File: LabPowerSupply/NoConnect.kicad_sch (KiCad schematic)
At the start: 2 parts

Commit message: another commit
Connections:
- net GND1: now reaches Inverter1.11
- net GND1: now also Inverter1.13, Inverter1.3, Inverter1.5, Inverter1.9
- net GND2: now reaches Inverter2.9
- net GND2: now also Inverter2.11, Inverter2.13
- no-connect marks 16 -> 8
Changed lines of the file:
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@@
     (rev "1")
     (company "George Mason University")
-    (comment 4 "This sheet is for the invertes not used in the circuit.")
+    (comment 4 "This sheet is for the inverters not used in the circuit.")
+  )
+  (junction (at 102.87 78.74) (diameter 0) (color 0 0 0 0)
+  )
+  (junction (at 140.97 78.74) (diameter 0) (color 0 0 0 0)
+  )
+  (junction (at 102.87 120.65) (diameter 0) (color 0 0 0 0)
+  )
+  (junction (at 102.87 92.71) (diameter 0) (color 0 0 0 0)
+  )
+  (junction (at 102.87 106.68) (diameter 0) (color 0 0 0 0)
+  )
+  (junction (at 140.97 92.71) (diameter 0) (color 0 0 0 0)
   )
   (no_connect (at 118.11 78.74))
-  (no_connect (at 102.87 78.74))
-  (no_connect (at 102.87 64.77))
   (no_connect (at 118.11 64.77))
   (no_connect (at 156.21 64.77))
-  (no_connect (at 140.97 64.77))
-  (no_connect (at 140.97 78.74))
   (no_connect (at 156.21 78.74))
   (no_connect (at 156.21 92.71))
-  (no_connect (at 140.97 92.71))
-  (no_connect (at 102.87 120.65))
   (no_connect (at 118.11 120.65))
   (no_connect (at 118.11 106.68))
-  (no_connect (at 102.87 106.68))
-  (no_connect (at 102.87 92.71))
   (no_connect (at 118.11 92.71))
+  (wire (pts (xy 140.97 78.74) (xy 140.97 92.71))
+    (stroke (width 0) (type default) (color 0 0 0 0))
+  )
+  (wire (pts (xy 102.87 120.65) (xy 100.33 120.65))
+    (stroke (width 0) (type default) (color 0 0 0 0))
+  )
+  (wire (pts (xy 102.87 64.77) (xy 102.87 78.74))
+    (stroke (width 0) (type default) (color 0 0 0 0))
+  )
+  (wire (pts (xy 140.97 64.77) (xy 140.97 78.74))
+    (stroke (width 0) (type default) (color 0 0 0 0))
+  )
+  (wire (pts (xy 102.87 78.74) (xy 102.87 92.71))
+    (stroke (width 0) (type default) (color 0 0 0 0))
+  )
+  (wire (pts (xy 102.87 106.68) (xy 102.87 120.65))
+    (stroke (width 0) (type default) (color 0 0 0 0))
+  )
+  (wire (pts (xy 102.87 92.71) (xy 102.87 106.68))
+    (stroke (width 0) (type default) (color 0 0 0 0))
+  )
+  (wire (pts (xy 140.97 92.71) (xy 138.43 92.71))
+    (stroke (width 0) (type default) (color 0 0 0 0))
+  )
+  (hierarchical_label "GND2" (shape input) (at 138.43 92.71 180)
+    (effects (font (size 1.27 1.27)) (justify right))
+  )
+  (hierarchical_label "GND1" (shape input) (at 100.33 120.65 180)
+    (effects (font (size 1.27 1.27)) (justify right))
+  )
   (symbol (lib_id "74xx:74AHC04") (at 110.49 106.68 0) (unit 5)
     (in_bom yes) (on_board yes) (fields_autoplaced)

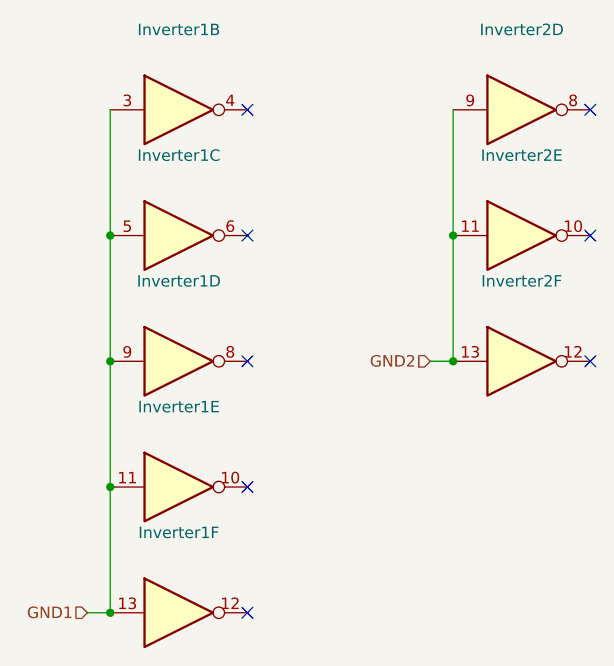
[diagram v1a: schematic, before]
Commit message: Made oscillator caps smd
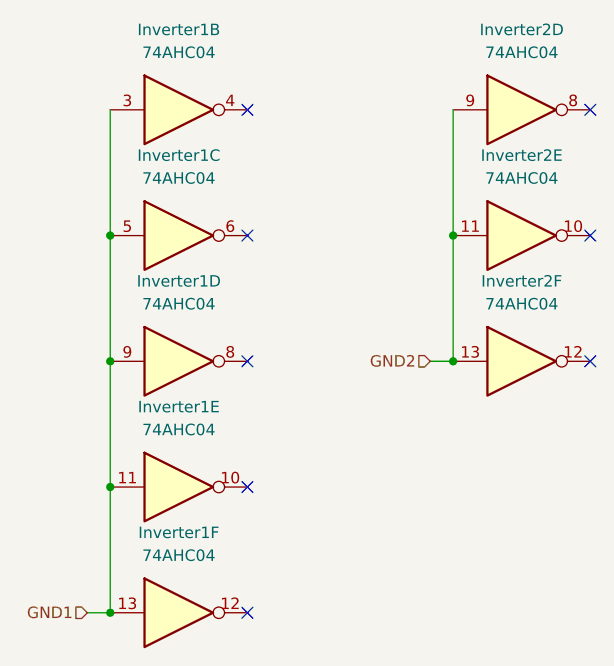
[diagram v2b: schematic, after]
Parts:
- Inverter1, Inverter2: value (none) -> 74AHC04; footprint (none) -> Package_DIP:DIP-14_W7.62mm
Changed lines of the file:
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@@
     (in_bom yes) (on_board yes) (fields_autoplaced)
     (property "Reference" "Inverter1" (id 0) (at 110.49 97.79 0))
-    (property "Value" "" (id 1) (at 110.49 100.33 0))
-    (property "Footprint" "" (id 2) (at 110.49 106.68 0)
+    (property "Value" "74AHC04" (id 1) (at 110.49 100.33 0))
+    (property "Footprint" "Package_DIP:DIP-14_W7.62mm" (id 2) (at 110.49 106.68 0)
       (effects (font (size 1.27 1.27)) hide)
     )
@@
     (in_bom yes) (on_board yes) (fields_autoplaced)
     (property "Reference" "Inverter1" (id 0) (at 110.49 111.76 0))
-    (property "Value" "" (id 1) (at 110.49 114.3 0))
-    (property "Footprint" "" (id 2) (at 110.49 120.65 0)
+    (property "Value" "74AHC04" (id 1) (at 110.49 114.3 0))
+    (property "Footprint" "Package_DIP:DIP-14_W7.62mm" (id 2) (at 110.49 120.65 0)
       (effects (font (size 1.27 1.27)) hide)
     )
@@
     (in_bom yes) (on_board yes) (fields_autoplaced)
     (property "Reference" "Inverter1" (id 0) (at 110.49 69.85 0))
-    (property "Value" "" (id 1) (at 110.49 72.39 0))
-    (property "Footprint" "" (id 2) (at 110.49 78.74 0)
+    (property "Value" "74AHC04" (id 1) (at 110.49 72.39 0))
+    (property "Footprint" "Package_DIP:DIP-14_W7.62mm" (id 2) (at 110.49 78.74 0)
       (effects (font (size 1.27 1.27)) hide)
     )
@@
     (in_bom yes) (on_board yes) (fields_autoplaced)
     (property "Reference" "Inverter1" (id 0) (at 110.49 55.88 0))
-    (property "Value" "" (id 1) (at 110.49 58.42 0))
-    (property "Footprint" "" (id 2) (at 110.49 64.77 0)
+    (property "Value" "74AHC04" (id 1) (at 110.49 58.42 0))
+    (property "Footprint" "Package_DIP:DIP-14_W7.62mm" (id 2) (at 110.49 64.77 0)
       (effects (font (size 1.27 1.27)) hide)
     )
@@
     (in_bom yes) (on_board yes) (fields_autoplaced)
     (property "Reference" "Inverter2" (id 0) (at 148.59 55.88 0))
-    (property "Value" "" (id 1) (at 148.59 58.42 0))
-    (property "Footprint" "" (id 2) (at 148.59 64.77 0)
+    (property "Value" "74AHC04" (id 1) (at 148.59 58.42 0))
+    (property "Footprint" "Package_DIP:DIP-14_W7.62mm" (id 2) (at 148.59 64.77 0)
       (effects (font (size 1.27 1.27)) hide)
     )
@@
     (in_bom yes) (on_board yes) (fields_autoplaced)
     (property "Reference" "Inverter2" (id 0) (at 148.59 69.85 0))
-    (property "Value" "" (id 1) (at 148.59 72.39 0))
-    (property "Footprint" "" (id 2) (at 148.59 78.74 0)
+    (property "Value" "74AHC04" (id 1) (at 148.59 72.39 0))
+    (property "Footprint" "Package_DIP:DIP-14_W7.62mm" (id 2) (at 148.59 78.74 0)
       (effects (font (size 1.27 1.27)) hide)
     )
@@
     (in_bom yes) (on_board yes) (fields_autoplaced)
     (property "Reference" "Inverter1" (id 0) (at 110.49 83.82 0))
-    (property "Value" "" (id 1) (at 110.49 86.36 0))
-    (property "Footprint" "" (id 2) (at 110.49 92.71 0)
+    (property "Value" "74AHC04" (id 1) (at 110.49 86.36 0))
+    (property "Footprint" "Package_DIP:DIP-14_W7.62mm" (id 2) (at 110.49 92.71 0)
       (effects (font (size 1.27 1.27)) hide)
     )
@@
     (in_bom yes) (on_board yes) (fields_autoplaced)
     (property "Reference" "Inverter2" (id 0) (at 148.59 83.82 0))
-    (property "Value" "" (id 1) (at 148.59 86.36 0))
-    (property "Footprint" "" (id 2) (at 148.59 92.71 0)
+    (property "Value" "74AHC04" (id 1) (at 148.59 86.36 0))
+    (property "Footprint" "Package_DIP:DIP-14_W7.62mm" (id 2) (at 148.59 92.71 0)
       (effects (font (size 1.27 1.27)) hide)
     )

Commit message: Changed most parts to smd
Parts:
- Inverter1: footprint Package_DIP:DIP-14_W7.62mm -> Package_SO:SSOP-14_5.3x6.2mm_P0.65mm
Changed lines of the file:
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@@
     (property "Reference" "Inverter1" (id 0) (at 110.49 97.79 0))
     (property "Value" "74AHC04" (id 1) (at 110.49 100.33 0))
-    (property "Footprint" "Package_DIP:DIP-14_W7.62mm" (id 2) (at 110.49 106.68 0)
+    (property "Footprint" "Package_SO:SSOP-14_5.3x6.2mm_P0.65mm" (id 2) (at 110.49 106.68 0)
       (effects (font (size 1.27 1.27)) hide)
     )
@@
     (property "Reference" "Inverter1" (id 0) (at 110.49 111.76 0))
     (property "Value" "74AHC04" (id 1) (at 110.49 114.3 0))
-    (property "Footprint" "Package_DIP:DIP-14_W7.62mm" (id 2) (at 110.49 120.65 0)
+    (property "Footprint" "Package_SO:SSOP-14_5.3x6.2mm_P0.65mm" (id 2) (at 110.49 120.65 0)
       (effects (font (size 1.27 1.27)) hide)
     )
@@
     (property "Reference" "Inverter1" (id 0) (at 110.49 69.85 0))
     (property "Value" "74AHC04" (id 1) (at 110.49 72.39 0))
-    (property "Footprint" "Package_DIP:DIP-14_W7.62mm" (id 2) (at 110.49 78.74 0)
+    (property "Footprint" "Package_SO:SSOP-14_5.3x6.2mm_P0.65mm" (id 2) (at 110.49 78.74 0)
       (effects (font (size 1.27 1.27)) hide)
     )
@@
     (property "Reference" "Inverter1" (id 0) (at 110.49 55.88 0))
     (property "Value" "74AHC04" (id 1) (at 110.49 58.42 0))
-    (property "Footprint" "Package_DIP:DIP-14_W7.62mm" (id 2) (at 110.49 64.77 0)
+    (property "Footprint" "Package_SO:SSOP-14_5.3x6.2mm_P0.65mm" (id 2) (at 110.49 64.77 0)
       (effects (font (size 1.27 1.27)) hide)
     )
@@
     (property "Reference" "Inverter1" (id 0) (at 110.49 83.82 0))
     (property "Value" "74AHC04" (id 1) (at 110.49 86.36 0))
-    (property "Footprint" "Package_DIP:DIP-14_W7.62mm" (id 2) (at 110.49 92.71 0)
+    (property "Footprint" "Package_SO:SSOP-14_5.3x6.2mm_P0.65mm" (id 2) (at 110.49 92.71 0)
       (effects (font (size 1.27 1.27)) hide)
     )

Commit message: routing is weird
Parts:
- Inverter2: footprint Package_DIP:DIP-14_W7.62mm -> Package_SO:SSOP-14_5.3x6.2mm_P0.65mm
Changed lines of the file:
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@@
     (property "Reference" "Inverter2" (id 0) (at 148.59 55.88 0))
     (property "Value" "74AHC04" (id 1) (at 148.59 58.42 0))
-    (property "Footprint" "Package_DIP:DIP-14_W7.62mm" (id 2) (at 148.59 64.77 0)
+    (property "Footprint" "Package_SO:SSOP-14_5.3x6.2mm_P0.65mm" (id 2) (at 148.59 64.77 0)
       (effects (font (size 1.27 1.27)) hide)
     )
@@
     (property "Reference" "Inverter2" (id 0) (at 148.59 69.85 0))
     (property "Value" "74AHC04" (id 1) (at 148.59 72.39 0))
-    (property "Footprint" "Package_DIP:DIP-14_W7.62mm" (id 2) (at 148.59 78.74 0)
+    (property "Footprint" "Package_SO:SSOP-14_5.3x6.2mm_P0.65mm" (id 2) (at 148.59 78.74 0)
       (effects (font (size 1.27 1.27)) hide)
     )
@@
     (property "Reference" "Inverter2" (id 0) (at 148.59 83.82 0))
     (property "Value" "74AHC04" (id 1) (at 148.59 86.36 0))
-    (property "Footprint" "Package_DIP:DIP-14_W7.62mm" (id 2) (at 148.59 92.71 0)
+    (property "Footprint" "Package_SO:SSOP-14_5.3x6.2mm_P0.65mm" (id 2) (at 148.59 92.71 0)
       (effects (font (size 1.27 1.27)) hide)
     )

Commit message: Ch2 restructure cont
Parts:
- added unit 2 of Inverter2
- added unit 3 of Inverter2
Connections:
- net GND2: now also Inverter2.3, Inverter2.5
- no-connect marks 8 -> 10
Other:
- moved on the sheet: Inverter2D, Inverter2E, Inverter2F
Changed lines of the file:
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@@
   (junction (at 102.87 78.74) (diameter 0) (color 0 0 0 0)
   )
+  (junction (at 140.97 106.68) (diameter 0) (color 0 0 0 0)
+  )
+  (junction (at 102.87 120.65) (diameter 0) (color 0 0 0 0)
+  )
+  (junction (at 102.87 92.71) (diameter 0) (color 0 0 0 0)
+  )
+  (junction (at 102.87 106.68) (diameter 0) (color 0 0 0 0)
+  )
+  (junction (at 140.97 92.71) (diameter 0) (color 0 0 0 0)
+  )
   (junction (at 140.97 78.74) (diameter 0) (color 0 0 0 0)
   )
-  (junction (at 102.87 120.65) (diameter 0) (color 0 0 0 0)
-  )
-  (junction (at 102.87 92.71) (diameter 0) (color 0 0 0 0)
-  )
-  (junction (at 102.87 106.68) (diameter 0) (color 0 0 0 0)
-  )
-  (junction (at 140.97 92.71) (diameter 0) (color 0 0 0 0)
-  )
+  (junction (at 140.97 120.65) (diameter 0) (color 0 0 0 0)
+  )
+  (no_connect (at 156.21 64.77))
   (no_connect (at 118.11 78.74))
   (no_connect (at 118.11 64.77))
-  (no_connect (at 156.21 64.77))
-  (no_connect (at 156.21 78.74))
   (no_connect (at 156.21 92.71))
+  (no_connect (at 156.21 106.68))
+  (no_connect (at 156.21 120.65))
   (no_connect (at 118.11 120.65))
   (no_connect (at 118.11 106.68))
   (no_connect (at 118.11 92.71))
+  (no_connect (at 156.21 78.74))
+  (wire (pts (xy 140.97 64.77) (xy 140.97 78.74))
+    (stroke (width 0) (type default) (color 0 0 0 0))
+  )
+  (wire (pts (xy 140.97 106.68) (xy 140.97 120.65))
+    (stroke (width 0) (type default) (color 0 0 0 0))
+  )
+  (wire (pts (xy 102.87 120.65) (xy 100.33 120.65))
+    (stroke (width 0) (type default) (color 0 0 0 0))
+  )
+  (wire (pts (xy 102.87 64.77) (xy 102.87 78.74))
+    (stroke (width 0) (type default) (color 0 0 0 0))
+  )
+  (wire (pts (xy 140.97 92.71) (xy 140.97 106.68))
+    (stroke (width 0) (type default) (color 0 0 0 0))
+  )
+  (wire (pts (xy 102.87 78.74) (xy 102.87 92.71))
+    (stroke (width 0) (type default) (color 0 0 0 0))
+  )
   (wire (pts (xy 140.97 78.74) (xy 140.97 92.71))
     (stroke (width 0) (type default) (color 0 0 0 0))
   )
-  (wire (pts (xy 102.87 120.65) (xy 100.33 120.65))
-    (stroke (width 0) (type default) (color 0 0 0 0))
-  )
-  (wire (pts (xy 102.87 64.77) (xy 102.87 78.74))
-    (stroke (width 0) (type default) (color 0 0 0 0))
-  )
-  (wire (pts (xy 140.97 64.77) (xy 140.97 78.74))
-    (stroke (width 0) (type default) (color 0 0 0 0))
-  )
-  (wire (pts (xy 102.87 78.74) (xy 102.87 92.71))
-    (stroke (width 0) (type default) (color 0 0 0 0))
-  )
   (wire (pts (xy 102.87 106.68) (xy 102.87 120.65))
     (stroke (width 0) (type default) (color 0 0 0 0))
@@
     (stroke (width 0) (type default) (color 0 0 0 0))
   )
-  (wire (pts (xy 140.97 92.71) (xy 138.43 92.71))
-    (stroke (width 0) (type default) (color 0 0 0 0))
-  )
-  (hierarchical_label "GND2" (shape input) (at 138.43 92.71 180)
+  (wire (pts (xy 140.97 120.65) (xy 138.43 120.65))
+    (stroke (width 0) (type default) (color 0 0 0 0))
+  )
+  (hierarchical_label "GND2" (shape input) (at 138.43 120.65 180)
     (effects (font (size 1.27 1.27)) (justify right))
   )
@@
     (pin "7")
   )
-  (symbol (lib_id "74xx:74AHC04") (at 148.59 64.77 0) (unit 4)
+  (symbol (lib_id "74xx:74AHC04") (at 148.59 92.71 0) (unit 4)
+    (in_bom yes) (on_board yes) (fields_autoplaced)
+    (property "Reference" "Inverter2" (id 0) (at 148.59 83.82 0))
+    (property "Value" "74AHC04" (id 1) (at 148.59 86.36 0))
+    (property "Footprint" "Package_SO:SSOP-14_5.3x6.2mm_P0.65mm" (id 2) (at 148.59 92.71 0)
+      (effects (font (size 1.27 1.27)) hide)
+    )
+    (property "Datasheet" "https://assets.nexperia.com/documents/data-sheet/74AHC_AHCT04.pdf" (id 3) (at 148.59 92.71 0)
+      (effects (font (size 1.27 1.27)) hide)
+    )
+    (pin "1")
+    (pin "2")
+    (pin "3")
+    (pin "4")
+    (pin "5")
+    (pin "6")
+    (pin "8")
+    (pin "9")
+    (pin "10")
+    (pin "11")
+    (pin "12")
+    (pin "13")
+    (pin "14")
+    (pin "7")
+  )
+  (symbol (lib_id "74xx:74AHC04") (at 148.59 64.77 0) (unit 2)
     (in_bom yes) (on_board yes) (fields_autoplaced)
     (property "Reference" "Inverter2" (id 0) (at 148.59 55.88 0))
@@
     (pin "7")
   )
-  (symbol (lib_id "74xx:74AHC04") (at 148.59 78.74 0) (unit 5)
+  (symbol (lib_id "74xx:74AHC04") (at 148.59 106.68 0) (unit 5)
+    (in_bom yes) (on_board yes) (fields_autoplaced)
+    (property "Reference" "Inverter2" (id 0) (at 148.59 97.79 0))
+    (property "Value" "74AHC04" (id 1) (at 148.59 100.33 0))
+    (property "Footprint" "Package_SO:SSOP-14_5.3x6.2mm_P0.65mm" (id 2) (at 148.59 106.68 0)
+      (effects (font (size 1.27 1.27)) hide)
+    )
+    (property "Datasheet" "https://assets.nexperia.com/documents/data-sheet/74AHC_AHCT04.pdf" (id 3) (at 148.59 106.68 0)
+      (effects (font (size 1.27 1.27)) hide)
+    )
+    (pin "1")
+    (pin "2")
+    (pin "3")
+    (pin "4")
+    (pin "5")
+    (pin "6")
+    (pin "8")
+    (pin "9")
+    (pin "10")
+    (pin "11")
+    (pin "12")
+    (pin "13")
+    (pin "14")
+    (pin "7")
+  )
+  (symbol (lib_id "74xx:74AHC04") (at 110.49 92.71 0) (unit 4)
+    (in_bom yes) (on_board yes) (fields_autoplaced)
+    (property "Reference" "Inverter1" (id 0) (at 110.49 83.82 0))
+    (property "Value" "74AHC04" (id 1) (at 110.49 86.36 0))
+    (property "Footprint" "Package_SO:SSOP-14_5.3x6.2mm_P0.65mm" (id 2) (at 110.49 92.71 0)
+      (effects (font (size 1.27 1.27)) hide)
+    )
+    (property "Datasheet" "https://assets.nexperia.com/documents/data-sheet/74AHC_AHCT04.pdf" (id 3) (at 110.49 92.71 0)
+      (effects (font (size 1.27 1.27)) hide)
+    )
+    (pin "1")
+    (pin "2")
+    (pin "3")
+    (pin "4")
+    (pin "5")
+    (pin "6")
+    (pin "8")
+    (pin "9")
+    (pin "10")
+    (pin "11")
+    (pin "12")
+    (pin "13")
+    (pin "14")
+    (pin "7")
+  )
+  (symbol (lib_id "74xx:74AHC04") (at 148.59 120.65 0) (unit 6)
+    (in_bom yes) (on_board yes) (fields_autoplaced)
+    (property "Reference" "Inverter2" (id 0) (at 148.59 111.76 0))
+    (property "Value" "74AHC04" (id 1) (at 148.59 114.3 0))
+    (property "Footprint" "Package_SO:SSOP-14_5.3x6.2mm_P0.65mm" (id 2) (at 148.59 120.65 0)
+      (effects (font (size 1.27 1.27)) hide)
+    )
+    (property "Datasheet" "https://assets.nexperia.com/documents/data-sheet/74AHC_AHCT04.pdf" (id 3) (at 148.59 120.65 0)
+      (effects (font (size 1.27 1.27)) hide)
+    )
+    (pin "1")
+    (pin "2")
+    (pin "3")
+    (pin "4")
+    (pin "5")
+    (pin "6")
+    (pin "8")
+    (pin "9")
+    (pin "10")
+    (pin "11")
+    (pin "12")
+    (pin "13")
+    (pin "14")
+    (pin "7")
+  )
+  (symbol (lib_id "74xx:74AHC04") (at 148.59 78.74 0) (unit 3)
     (in_bom yes) (on_board yes) (fields_autoplaced)
     (property "Reference" "Inverter2" (id 0) (at 148.59 69.85 0))
@@
       (effects (font (size 1.27 1.27)) hide)
     )
-    (pin "1")
-    (pin "2")
-    (pin "3")
-    (pin "4")
-    (pin "5")
-    (pin "6")
-    (pin "8")
-    (pin "9")
-    (pin "10")
-    (pin "11")
-    (pin "12")
-    (pin "13")
-    (pin "14")
-    (pin "7")
-  )
-  (symbol (lib_id "74xx:74AHC04") (at 110.49 92.71 0) (unit 4)
-    (in_bom yes) (on_board yes) (fields_autoplaced)
-    (property "Reference" "Inverter1" (id 0) (at 110.49 83.82 0))
-    (property "Value" "74AHC04" (id 1) (at 110.49 86.36 0))
-    (property "Footprint" "Package_SO:SSOP-14_5.3x6.2mm_P0.65mm" (id 2) (at 110.49 92.71 0)
-      (effects (font (size 1.27 1.27)) hide)
-    )
-    (property "Datasheet" "https://assets.nexperia.com/documents/data-sheet/74AHC_AHCT04.pdf" (id 3) (at 110.49 92.71 0)
-      (effects (font (size 1.27 1.27)) hide)
-    )
-    (pin "1")
-    (pin "2")
-    (pin "3")
-    (pin "4")
-    (pin "5")
-    (pin "6")
-    (pin "8")
-    (pin "9")
-    (pin "10")
-    (pin "11")
-    (pin "12")
-    (pin "13")
-    (pin "14")
-    (pin "7")
-  )
-  (symbol (lib_id "74xx:74AHC04") (at 148.59 92.71 0) (unit 6)
-    (in_bom yes) (on_board yes) (fields_autoplaced)
-    (property "Reference" "Inverter2" (id 0) (at 148.59 83.82 0))
-    (property "Value" "74AHC04" (id 1) (at 148.59 86.36 0))
-    (property "Footprint" "Package_SO:SSOP-14_5.3x6.2mm_P0.65mm" (id 2) (at 148.59 92.71 0)
-      (effects (font (size 1.27 1.27)) hide)
-    )
-    (property "Datasheet" "https://assets.nexperia.com/documents/data-sheet/74AHC_AHCT04.pdf" (id 3) (at 148.59 92.71 0)
-      (effects (font (size 1.27 1.27)) hide)
-    )
